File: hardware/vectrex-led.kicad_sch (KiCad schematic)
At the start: 10 parts

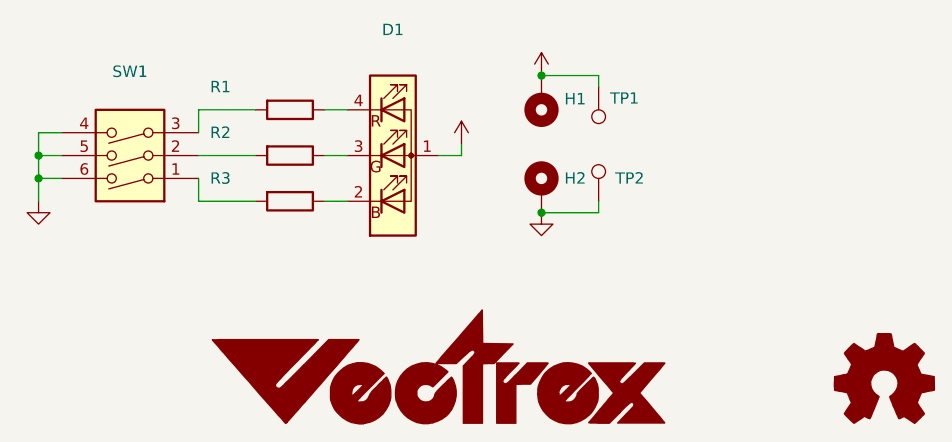
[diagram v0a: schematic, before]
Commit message: update RGB LED resistor values for deeper color
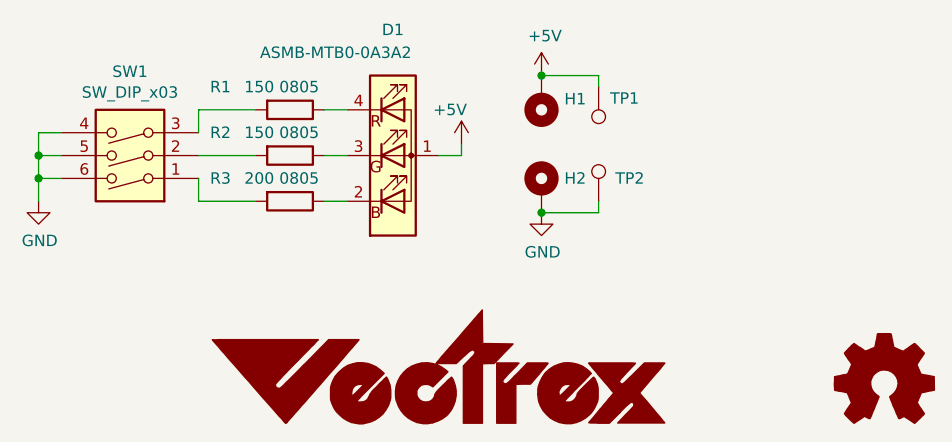
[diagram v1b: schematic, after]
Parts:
- D1: value (none) -> ASMB-MTB0-0A3A2; footprint (none) -> vectrex-cartridge:LED_Avago_PLCC4_3.2x2.8mm_CW
- G1: value (none) -> LOGO; footprint (none) -> vectrex-cartridge:vectrex-us-soldermask-15mm
- H1, H2: value (none) -> MountingHole_Pad; footprint (none) -> TestPoint:TestPoint_THTPad_D2.0mm_Drill1.0mm
- R1, R2: value (none) -> 150 0805; footprint (none) -> Resistor_SMD:R_0805_2012Metric_Pad1.15x1.40mm_HandSolder
- R3: value (none) -> 200 0805; footprint (none) -> Resistor_SMD:R_0805_2012Metric_Pad1.15x1.40mm_HandSolder
- SW1: value (none) -> SW_DIP_x03; footprint (none) -> Button_Switch_SMD:SW_DIP_SPSTx03_Slide_6.7x9.18mm_W8.61mm_P2.54mm_LowProfile
- TP1, TP2: value (none) -> TestPoint; footprint (none) -> TestPoint:TestPoint_Pad_D2.0mm
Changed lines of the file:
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@@
       (effects (font (size 1.27 1.27)) hide)
     )
-    (property "Value" "" (id 1) (at 278.13 180.975 0)
+    (property "Value" "Logo_Open_Hardware_Small" (id 1) (at 278.13 180.975 0)
       (effects (font (size 1.27 1.27)) hide)
     )
@@
       (effects (font (size 1.27 1.27)) hide)
     )
-    (property "Value" "" (id 1) (at 240.157 160.6042 0))
+    (property "Value" "GND" (id 1) (at 240.157 160.6042 0))
     (property "Footprint" "" (id 2) (at 240.03 156.21 0)
       (effects (font (size 1.27 1.27)) hide)
@@
     (in_bom yes) (on_board yes)
     (property "Reference" "D1" (id 0) (at 223.52 135.89 0))
-    (property "Value" "" (id 1) (at 217.17 138.43 0))
-    (property "Footprint" "" (id 2) (at 223.52 137.16 0)
+    (property "Value" "ASMB-MTB0-0A3A2" (id 1) (at 217.17 138.43 0))
+    (property "Footprint" "vectrex-cartridge:LED_Avago_PLCC4_3.2x2.8mm_CW" (id 2) (at 223.52 137.16 0)
       (effects (font (size 1.27 1.27)) hide)
     )
@@
       (effects (font (size 1.27 1.27)) (justify left))
     )
-    (property "Value" "" (id 1) (at 207.01 142.24 90)
-      (effects (font (size 1.27 1.27)) (justify left))
-    )
-    (property "Footprint" "" (id 2) (at 212.09 143.002 90)
+    (property "Value" "150 0805" (id 1) (at 207.01 142.24 90)
+      (effects (font (size 1.27 1.27)) (justify left))
+    )
+    (property "Footprint" "Resistor_SMD:R_0805_2012Metric_Pad1.15x1.40mm_HandSolder" (id 2) (at 212.09 143.002 90)
       (effects (font (size 1.27 1.27)) hide)
     )
@@
       (effects (font (size 1.27 1.27)) (justify left))
     )
-    (property "Value" "" (id 1) (at 207.01 147.32 90)
-      (effects (font (size 1.27 1.27)) (justify left))
-    )
-    (property "Footprint" "" (id 2) (at 212.09 148.082 90)
+    (property "Value" "150 0805" (id 1) (at 207.01 147.32 90)
+      (effects (font (size 1.27 1.27)) (justify left))
+    )
+    (property "Footprint" "Resistor_SMD:R_0805_2012Metric_Pad1.15x1.40mm_HandSolder" (id 2) (at 212.09 148.082 90)
       (effects (font (size 1.27 1.27)) hide)
     )
@@
       (effects (font (size 1.27 1.27)) (justify left))
     )
-    (property "Value" "" (id 1) (at 207.01 152.4 90)
-      (effects (font (size 1.27 1.27)) (justify left))
-    )
-    (property "Footprint" "" (id 2) (at 212.09 153.162 90)
+    (property "Value" "200 0805" (id 1) (at 207.01 152.4 90)
+      (effects (font (size 1.27 1.27)) (justify left))
+    )
+    (property "Footprint" "Resistor_SMD:R_0805_2012Metric_Pad1.15x1.40mm_HandSolder" (id 2) (at 212.09 153.162 90)
       (effects (font (size 1.27 1.27)) hide)
     )
@@
       (effects (font (size 1.27 1.27)) hide)
     )
-    (property "Value" "" (id 1) (at 184.277 159.3342 0))
+    (property "Value" "GND" (id 1) (at 184.277 159.3342 0))
     (property "Footprint" "" (id 2) (at 184.15 154.94 0)
       (effects (font (size 1.27 1.27)) hide)
@@
       (effects (font (size 1.27 1.27)) hide)
     )
-    (property "Value" "" (id 1) (at 229.87 144.78 0))
+    (property "Value" "+5V" (id 1) (at 229.87 144.78 0))
     (property "Footprint" "" (id 2) (at 231.14 148.59 0)
       (effects (font (size 1.27 1.27)) hide)
@@
       (effects (font (size 1.27 1.27)) (justify left))
     )
-    (property "Value" "" (id 1) (at 242.57 154.7368 0)
+    (property "Value" "MountingHole_Pad" (id 1) (at 242.57 154.7368 0)
       (effects (font (size 1.27 1.27)) (justify left) hide)
     )
-    (property "Footprint" "" (id 2) (at 240.03 153.67 0)
+    (property "Footprint" "TestPoint:TestPoint_THTPad_D2.0mm_Drill1.0mm" (id 2) (at 240.03 153.67 0)
       (effects (font (size 1.27 1.27)) hide)
     )
@@
       (effects (font (size 1.27 1.27)) (justify right))
     )
-    (property "Value" "" (id 1) (at 242.57 144.7292 0)
+    (property "Value" "MountingHole_Pad" (id 1) (at 242.57 144.7292 0)
       (effects (font (size 1.27 1.27)) (justify right) hide)
     )
-    (property "Footprint" "" (id 2) (at 240.03 143.51 0)
+    (property "Footprint" "TestPoint:TestPoint_THTPad_D2.0mm_Drill1.0mm" (id 2) (at 240.03 143.51 0)
       (effects (font (size 1.27 1.27)) hide)
     )
@@
       (effects (font (size 1.27 1.27)) hide)
     )
-    (property "Value" "" (id 1) (at 240.411 136.5758 0))
+    (property "Value" "+5V" (id 1) (at 240.411 136.5758 0))
     (property "Footprint" "" (id 2) (at 240.03 140.97 0)
       (effects (font (size 1.27 1.27)) hide)
@@
     (in_bom yes) (on_board yes)
     (property "Reference" "SW1" (id 0) (at 194.31 140.5382 0))
-    (property "Value" "" (id 1) (at 194.31 142.8496 0))
-    (property "Footprint" "" (id 2) (at 194.31 147.32 0)
+    (property "Value" "SW_DIP_x03" (id 1) (at 194.31 142.8496 0))
+    (property "Footprint" "Button_Switch_SMD:SW_DIP_SPSTx03_Slide_6.7x9.18mm_W8.61mm_P2.54mm_LowProfile" (id 2) (at 194.31 147.32 0)
       (effects (font (size 1.27 1.27)) hide)
     )
@@
       (effects (font (size 1.524 1.524)) hide)
     )
-    (property "Value" "" (id 1) (at 228.6 167.767 0)
+    (property "Value" "LOGO" (id 1) (at 228.6 167.767 0)
       (effects (font (size 1.524 1.524)) hide)
     )
-    (property "Footprint" "" (id 2) (at 228.6 173.355 0)
+    (property "Footprint" "vectrex-cartridge:vectrex-us-soldermask-15mm" (id 2) (at 228.6 173.355 0)
       (effects (font (size 1.27 1.27)) hide)
     )
@@
       (effects (font (size 1.27 1.27)) (justify right))
     )
-    (property "Value" "" (id 1) (at 247.8532 145.2118 0)
+    (property "Value" "TestPoint" (id 1) (at 247.8532 145.2118 0)
       (effects (font (size 1.27 1.27)) (justify right) hide)
     )
-    (property "Footprint" "" (id 2) (at 241.3 142.24 0)
+    (property "Footprint" "TestPoint:TestPoint_Pad_D2.0mm" (id 2) (at 241.3 142.24 0)
       (effects (font (size 1.27 1.27)) hide)
     )
@@
       (effects (font (size 1.27 1.27)) (justify right))
     )
-    (property "Value" "" (id 1) (at 244.9068 151.9682 0)
+    (property "Value" "TestPoint" (id 1) (at 244.9068 151.9682 0)
       (effects (font (size 1.27 1.27)) (justify right) hide)
     )
-    (property "Footprint" "" (id 2) (at 251.46 154.94 0)
+    (property "Footprint" "TestPoint:TestPoint_Pad_D2.0mm" (id 2) (at 251.46 154.94 0)
       (effects (font (size 1.27 1.27)) hide)
     )
@@
     )
     (path "/00000000-0000-0000-0000-00005ef83871"
-      (reference "R1") (unit 1) (value "200 0805") (footprint "Resistor_SMD:R_0805_2012Metric_Pad1.15x1.40mm_HandSolder")
+      (reference "R1") (unit 1) (value "150 0805") (footprint "Resistor_SMD:R_0805_2012Metric_Pad1.15x1.40mm_HandSolder")
     )
     (path "/00000000-0000-0000-0000-00005ef84abe"
-      (reference "R2") (unit 1) (value "200 0805") (footprint "Resistor_SMD:R_0805_2012Metric_Pad1.15x1.40mm_HandSolder")
+      (reference "R2") (unit 1) (value "150 0805") (footprint "Resistor_SMD:R_0805_2012Metric_Pad1.15x1.40mm_HandSolder")
     )
     (path "/00000000-0000-0000-0000-00005ef84e8a"
-      (reference "R3") (unit 1) (value "120 0805") (footprint "Resistor_SMD:R_0805_2012Metric_Pad1.15x1.40mm_HandSolder")
+      (reference "R3") (unit 1) (value "200 0805") (footprint "Resistor_SMD:R_0805_2012Metric_Pad1.15x1.40mm_HandSolder")
     )
     (path "/00000000-0000-0000-0000-00005efc1237"
